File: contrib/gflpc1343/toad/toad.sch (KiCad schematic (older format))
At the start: 0 parts

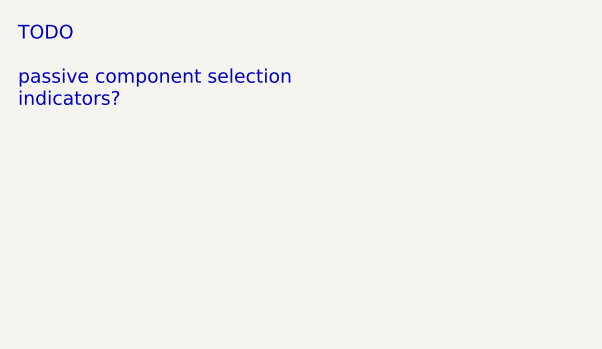
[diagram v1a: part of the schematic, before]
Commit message: TOAD: power indicator LED, some component selection
git-svn-id: https://svn.code.sf.net/p/goodfet/code@1623 12e2690d-a6be-4b82-a7b7-67c4a43b65c8
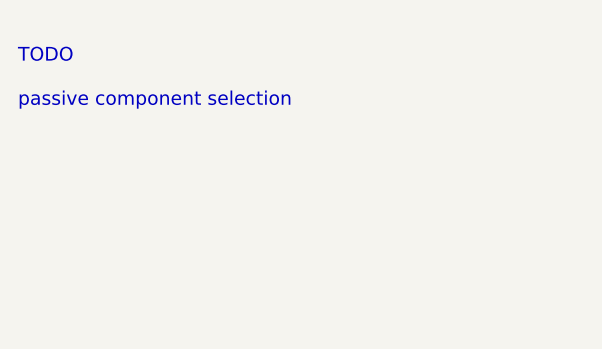
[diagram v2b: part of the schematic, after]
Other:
- note added: "TODO\n\npassive component selection"
- note removed: "TODO\n\npassive component selection\nindicators?"
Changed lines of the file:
@@
-EESchema Schematic File Version 2  date Sun Jul 14 16:16:23 2013
+EESchema Schematic File Version 2  date Mon Jul 15 21:49:01 2013
 LIBS:power
 LIBS:device
@@
 Sheet 1 4
 Title ""
-Date "14 jul 2013"
+Date "16 jul 2013"
 Rev ""
 Comp ""
@@
 $EndSheet
 Text Notes 1700 1250 0    60   ~ 0
-TODO\n\npassive component selection\nindicators?
+TODO\n\npassive component selection
 $Sheet
 S 4150 5850 2750 1000
